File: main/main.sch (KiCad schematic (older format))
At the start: 20 parts, among them J1 AC MAINS, J2 Molex 47054-1000, J5 PROGRAMMING, Q1 MMBT3904, U1 LM7805_TO220, U3 DS18B20, U4 ATtiny5-TS

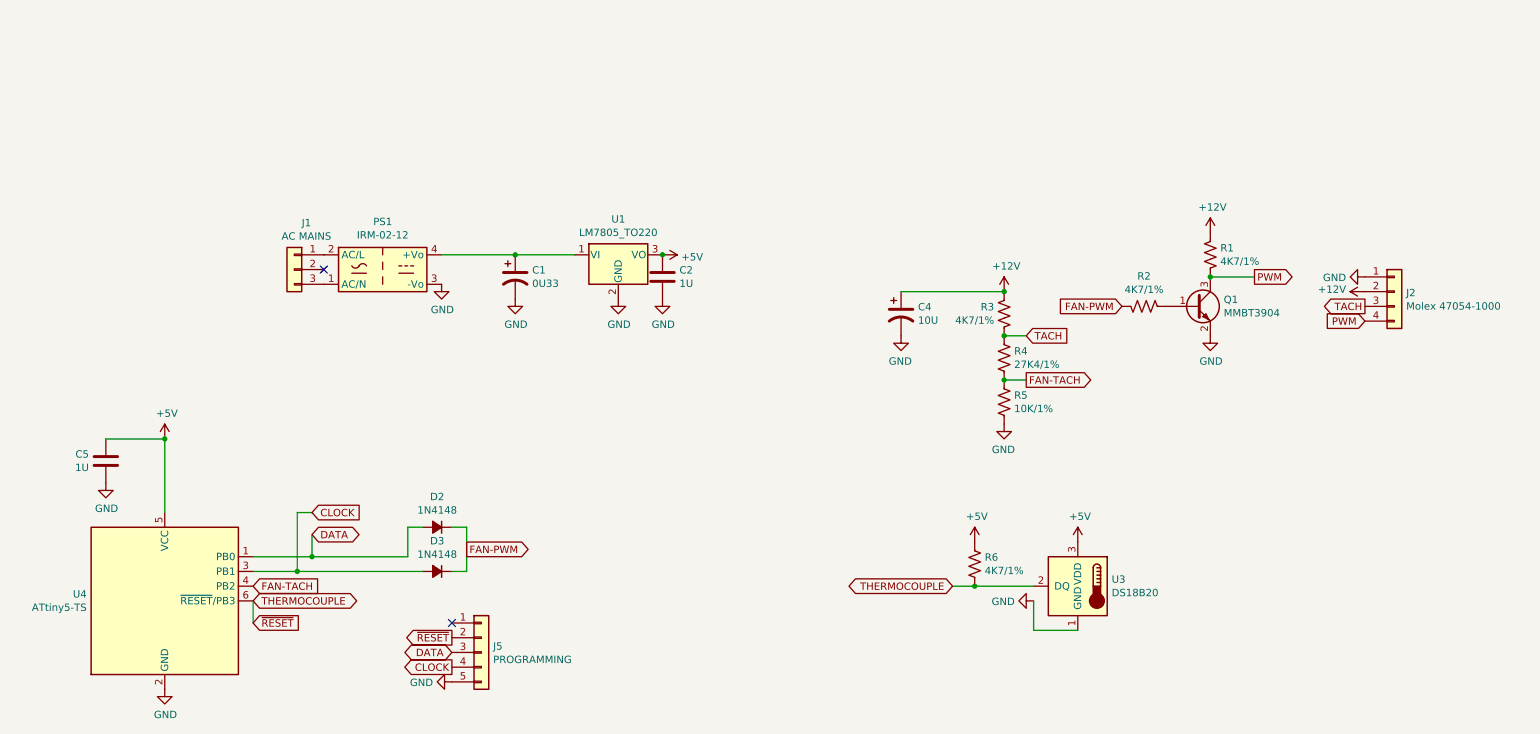
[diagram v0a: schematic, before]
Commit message: simpler power supply, and slightly better layout
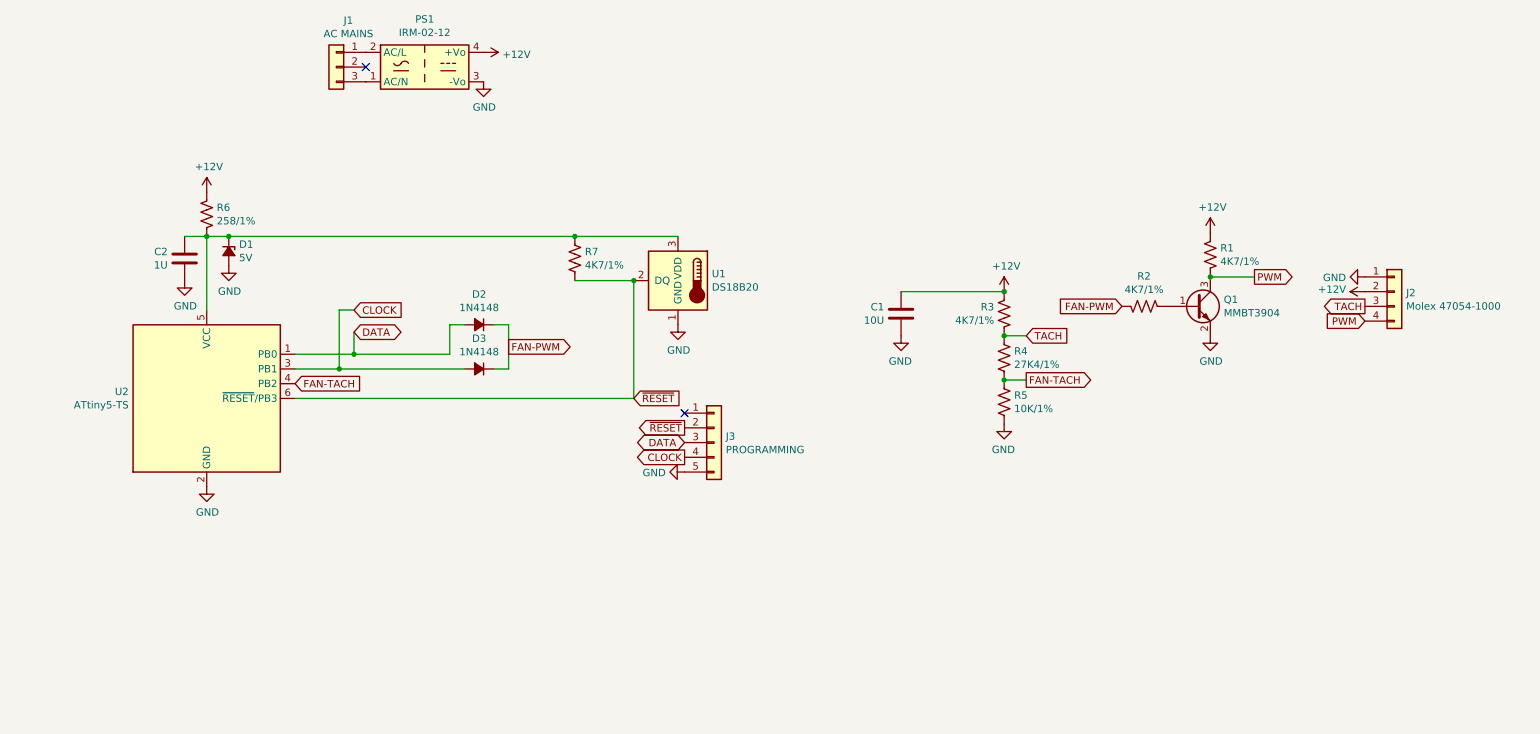
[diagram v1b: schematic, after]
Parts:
- removed C1: 0U33, Capacitor_SMD:CP_Elec_6.3x5.4_Nichicon, symbol Device:CP1
- removed C2: 1U, Capacitor_SMD:C_0603_1608Metric, symbol Device:C
- removed C4: 10U, Capacitor_SMD:CP_Elec_6.3x5.4_Nichicon, symbol Device:CP1
- removed U1: LM7805_TO220, Package_TO_SOT_THT:TO-220-3_Vertical, symbol Regulator_Linear:LM7805_TO220
- added C1: 10U, Capacitor_SMD:C_1206_3216Metric, symbol Device:C
- added D1: 5V, Diode_SMD:D_0603_1608Metric, symbol Device:D_Zener_Small_ALT
- added R6: 258/1%, Resistor_SMD:R_0805_2012Metric, symbol Device:R_US
- renumbered C5 to C2, J5 to J3, R6 to R7, U3 to U1, U4 to U2
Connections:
- net +12V: now also PS1.4 (+Vo), C1.2, R6.1
- net GND: now also C1.1, D1.2 (A)
- net +5V: no longer names the net of C2.2, R7.2, U1.3 (VDD), U2.5 (VCC)
- net +5V: now also D1.1 (K), R6.2
- net THERMOCOUPLE renamed ~RESET
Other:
- moved on the sheet: C2, D2, D3, J1, J3, PS1, R7, U1, U2

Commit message: simpler dumber fan controller, will add pwm feedback and temp sensing later
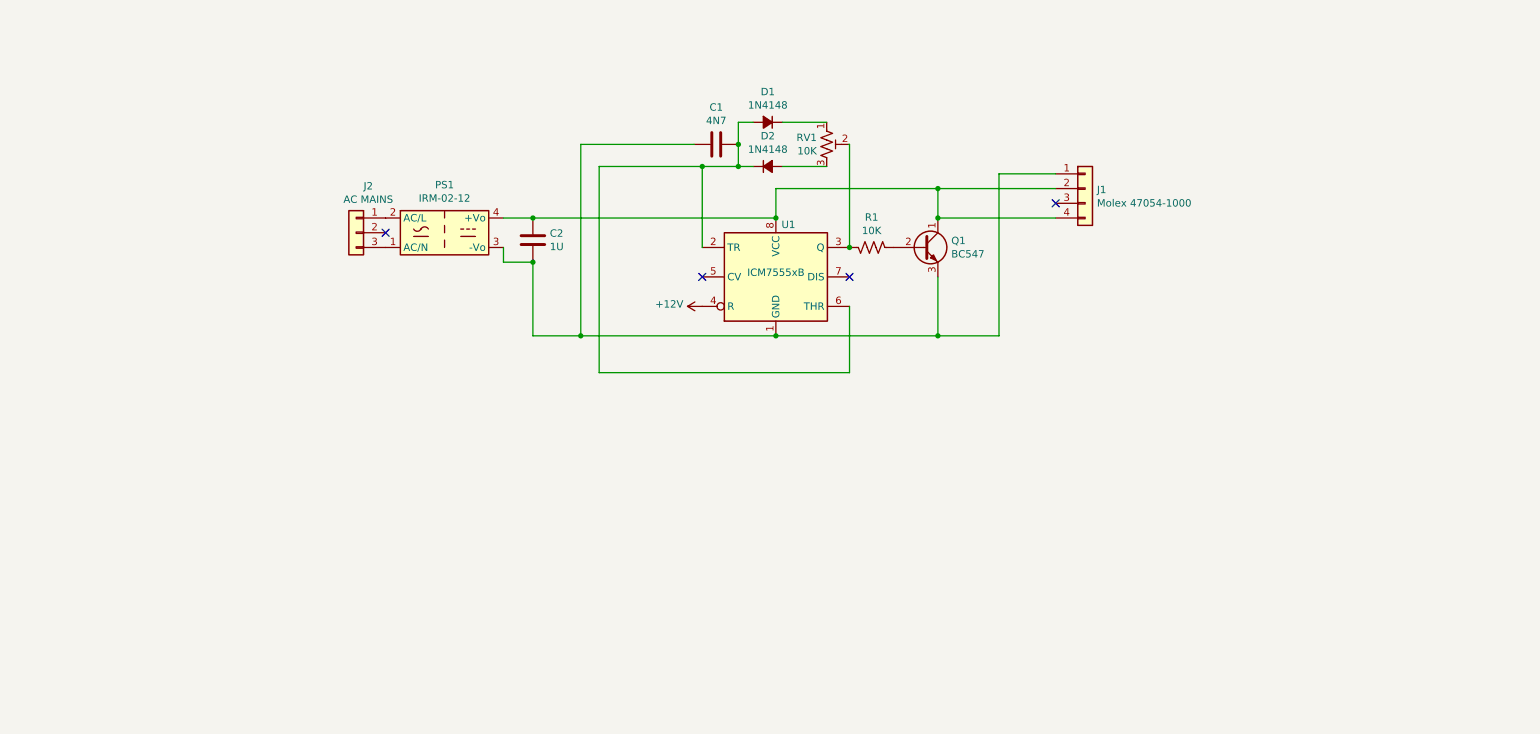
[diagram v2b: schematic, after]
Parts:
- removed D1: 5V, Diode_SMD:D_0603_1608Metric, symbol Device:D_Zener_Small_ALT
- removed D3: 1N4148, Diode_SMD:D_0603_1608Metric, symbol Device:D_Small_ALT
- removed J3: PROGRAMMING, Connector_PinHeader_2.54mm:PinHeader_1x05_P2.54mm_Vertical, symbol Connector_Generic:Conn_01x05
- removed Q1: MMBT3904, Package_TO_SOT_SMD:SOT-23, symbol Transistor_BJT:MMBT3904
- removed R1, R3, R7: 4K7/1%, Resistor_SMD:R_0805_2012Metric, symbol Device:R_US
- removed R4: 27K4/1%, Resistor_SMD:R_0805_2012Metric, symbol Device:R_US
- removed R5: 10K/1%, Resistor_SMD:R_0805_2012Metric, symbol Device:R_US
- removed R6: 258/1%, Resistor_SMD:R_0805_2012Metric, symbol Device:R_US
- removed U1: DS18B20, Package_TO_SOT_THT:TO-92_Inline, symbol Sensor_Temperature:DS18B20
- removed U2: ATtiny5-TS, Package_TO_SOT_SMD:SOT-23-6, symbol MCU_Microchip_ATtiny:ATtiny5-TS
- added D1: 1N4148, Diode_SMD:D_0603_1608Metric, symbol Device:D_Small_ALT
- added Q1: BC547, Package_TO_SOT_THT:TO-92_Inline, symbol Transistor_BJT:BC547
- added RV1: 10K, Potentiometer_SMD:Potentiometer_ACP_CA6-VSMD_Vertical, symbol Device:R_POT_TRIM_US
- added U1: ICM7555xB, Package_SO:SOIC-8_3.9x4.9mm_P1.27mm, symbol Timer:ICM7555xB
- C1: value 10U -> 4N7; footprint Capacitor_SMD:C_1206_3216Metric -> Capacitor_SMD:C_0805_2012Metric
- C2: footprint Capacitor_SMD:C_0603_1608Metric -> Capacitor_SMD:C_0805_2012Metric
- R1: renamed from R2; value 4K7/1% -> 10K
- renumbered J2 to J1, J1 to J2
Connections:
- net +12V: now also U1.4 (R); no longer C1.2, J1.2 (Pin_2), PS1.4 (+Vo)
- net at C2.2: now also C1.2, J1.1 (Pin_1), PS1.3 (-Vo), Q1.3 (E), U1.1 (GND)
- net at R1.2: now also Q1.2 (B)
- net DATA: no longer names the net of D2.2 (A)
- net DATA: now also RV1.3
- net FAN-PWM: no longer names the net of D2.1 (K)
- net FAN-PWM: now also C1.1, D1.2 (A), U1.2 (TR), U1.6 (THR); no longer R1.1
- removed net GND: C1.1, C2.1, J1.1 (Pin_1), PS1.3 (-Vo)
- net PWM: no longer names the net of J1.4 (Pin_4)
- net PWM: now also C2.1, J1.2 (Pin_2), PS1.4 (+Vo), Q1.1 (C), U1.8 (VCC)
- net TACH: no longer names the net of J1.3 (Pin_3)
- new net: D1.1 (K), RV1.1
- new net: R1.1, RV1.2, U1.3 (Q)
- no-connect marks 2 -> 4
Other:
- moved on the sheet: J1, J2, PS1, R1
